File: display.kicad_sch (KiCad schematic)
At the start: 42 parts, among them J301 FPC24(0.5MM), J302 FPC10(0.5MM), Q301 2N7002, Q302 2N7002, Q303 AO3401A

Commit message: Pre routing: footprints&parts
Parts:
- D301, D302, D303, D304, D305, D306: JLCPCB (none) -> C965863
- D307, D308, D309: value MDD SS14 -> B5819W; footprint Diode_SMD:D_SMA -> Diode_SMD:D_SOD-123; JLCPCB C2480 -> C8598
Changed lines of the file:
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@@
       (effects (font (size 1.27 1.27)) hide)
     )
-    (property "JLCPCB" "" (id 4) (at 78.105 140.97 0)
+    (property "JLCPCB" "C965863" (id 4) (at 78.105 140.97 0)
       (effects (font (size 1.27 1.27)) hide)
     )
@@
       (effects (font (size 1.27 1.27)) hide)
     )
-    (property "JLCPCB" "" (id 4) (at 78.105 62.23 0)
+    (property "JLCPCB" "C965863" (id 4) (at 78.105 62.23 0)
       (effects (font (size 1.27 1.27)) hide)
     )
@@
     (in_bom yes) (on_board yes)
     (property "Reference" "D308" (id 0) (at 171.45 49.403 0))
-    (property "Value" "MDD SS14" (id 1) (at 174.244 44.958 0))
-    (property "Footprint" "Diode_SMD:D_SMA" (id 2) (at 171.45 46.99 0)
-      (effects (font (size 1.27 1.27)) hide)
-    )
-    (property "Datasheet" "https://datasheet.lcsc.com/lcsc/2204121115_MDD-Microdiode-Electronics--SS14_C2480.pdf" (id 3) (at 171.45 46.99 0)
-      (effects (font (size 1.27 1.27)) hide)
-    )
-    (property "JLCPCB" "C2480" (id 4) (at 171.45 46.99 0)
+    (property "Value" "B5819W" (id 1) (at 174.244 44.958 0))
+    (property "Footprint" "Diode_SMD:D_SOD-123" (id 2) (at 171.45 46.99 0)
+      (effects (font (size 1.27 1.27)) hide)
+    )
+    (property "Datasheet" "" (id 3) (at 171.45 46.99 0)
+      (effects (font (size 1.27 1.27)) hide)
+    )
+    (property "JLCPCB" "C8598 " (id 4) (at 171.45 46.99 0)
       (effects (font (size 1.27 1.27)) hide)
     )
@@
     (in_bom yes) (on_board yes)
     (property "Reference" "D307" (id 0) (at 162.56 74.93 90))
-    (property "Value" "MDD SS14" (id 1) (at 166.37 72.39 90))
-    (property "Footprint" "Diode_SMD:D_SMA" (id 2) (at 160.02 72.39 0)
-      (effects (font (size 1.27 1.27)) hide)
-    )
-    (property "Datasheet" "https://datasheet.lcsc.com/lcsc/2204121115_MDD-Microdiode-Electronics--SS14_C2480.pdf" (id 3) (at 160.02 72.39 0)
-      (effects (font (size 1.27 1.27)) hide)
-    )
-    (property "JLCPCB" "C2480" (id 4) (at 160.02 72.39 0)
+    (property "Value" "B5819W" (id 1) (at 166.37 72.39 90))
+    (property "Footprint" "Diode_SMD:D_SOD-123" (id 2) (at 160.02 72.39 0)
+      (effects (font (size 1.27 1.27)) hide)
+    )
+    (property "Datasheet" "" (id 3) (at 160.02 72.39 0)
+      (effects (font (size 1.27 1.27)) hide)
+    )
+    (property "JLCPCB" "C8598 " (id 4) (at 160.02 72.39 0)
       (effects (font (size 1.27 1.27)) hide)
     )
@@
       (effects (font (size 1.27 1.27)) hide)
     )
-    (property "JLCPCB" "" (id 4) (at 107.315 62.23 0)
+    (property "JLCPCB" "C965863" (id 4) (at 107.315 62.23 0)
       (effects (font (size 1.27 1.27)) hide)
     )
@@
       (effects (font (size 1.27 1.27)) hide)
     )
-    (property "JLCPCB" "" (id 4) (at 92.71 140.97 0)
+    (property "JLCPCB" "C965863" (id 4) (at 92.71 140.97 0)
       (effects (font (size 1.27 1.27)) hide)
     )
@@
       (effects (font (size 1.27 1.27)) hide)
     )
-    (property "JLCPCB" "" (id 4) (at 92.71 62.23 0)
+    (property "JLCPCB" "C965863" (id 4) (at 92.71 62.23 0)
       (effects (font (size 1.27 1.27)) hide)
     )
@@
     (in_bom yes) (on_board yes)
     (property "Reference" "D309" (id 0) (at 172.085 69.85 0))
-    (property "Value" "MDD SS14" (id 1) (at 174.371 65.151 0))
-    (property "Footprint" "Diode_SMD:D_SMA" (id 2) (at 171.45 67.31 0)
-      (effects (font (size 1.27 1.27)) hide)
-    )
-    (property "Datasheet" "https://datasheet.lcsc.com/lcsc/2204121115_MDD-Microdiode-Electronics--SS14_C2480.pdf" (id 3) (at 171.45 67.31 0)
-      (effects (font (size 1.27 1.27)) hide)
-    )
-    (property "JLCPCB" "C2480" (id 4) (at 171.45 67.31 0)
+    (property "Value" "B5819W" (id 1) (at 174.371 65.151 0))
+    (property "Footprint" "Diode_SMD:D_SOD-123" (id 2) (at 171.45 67.31 0)
+      (effects (font (size 1.27 1.27)) hide)
+    )
+    (property "Datasheet" "" (id 3) (at 171.45 67.31 0)
+      (effects (font (size 1.27 1.27)) hide)
+    )
+    (property "JLCPCB" "C8598 " (id 4) (at 171.45 67.31 0)
       (effects (font (size 1.27 1.27)) hide)
     )
@@
       (effects (font (size 1.27 1.27)) hide)
     )
-    (property "JLCPCB" "" (id 4) (at 107.315 140.97 0)
-      (effects (font (size 1.27 1.27)) hide)
-    )
+    (property "JLCPCB" "C965863" (id 4) (at 107.315 140.97 0)
+      (effects (font (size 1.27 1.27)) hide)
+    )

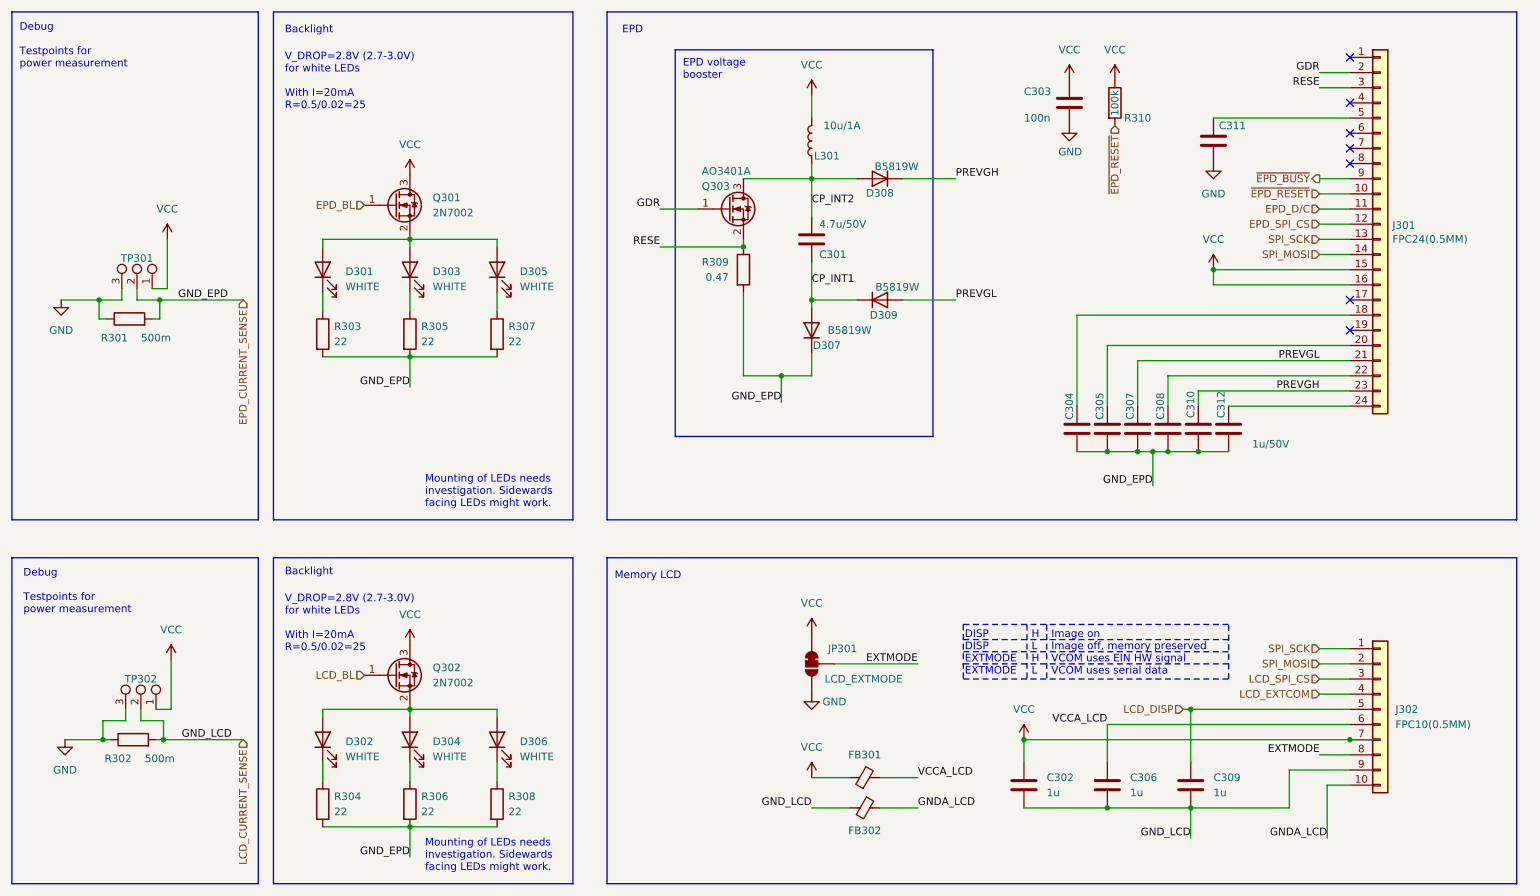
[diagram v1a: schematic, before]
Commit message: Schematics: Add mountingpins to connectors, remove ERC warnings for alternate parts
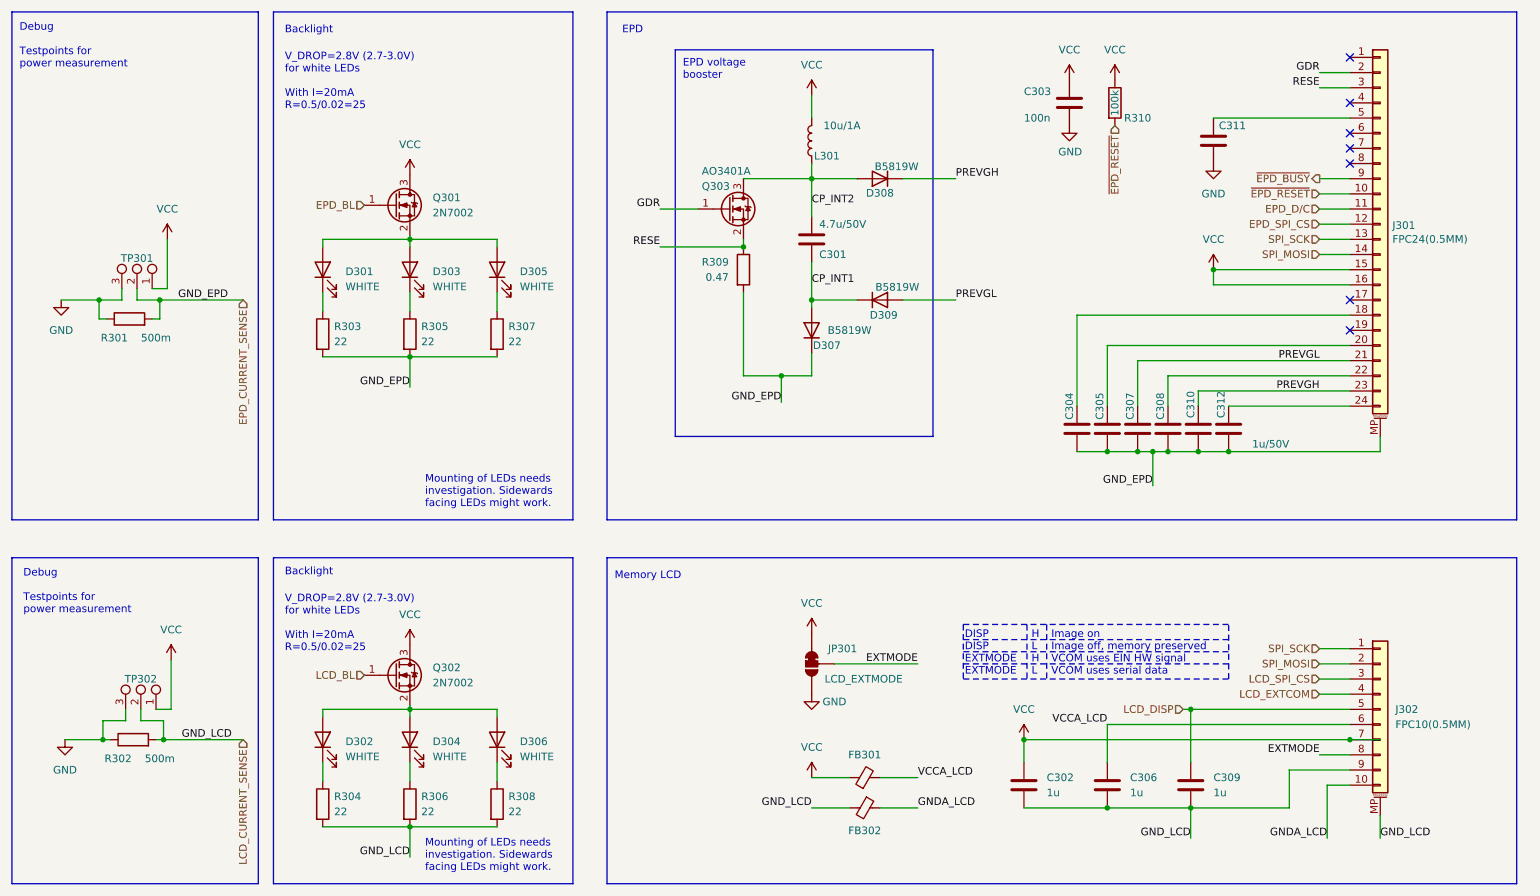
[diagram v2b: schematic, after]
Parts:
- D301, D302, D303, D304, D305, D306: footprint LED_SMD:LED_0805_2012Metric -> project-lib:LED_sidemount
- J301: symbol Connector_Generic:Conn_01x24 -> Connector_Generic_MountingPin:Conn_01x24_MountingPin
- J302: symbol Connector_Generic:Conn_01x10 -> Connector_Generic_MountingPin:Conn_01x10_MountingPin
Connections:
- net EPD_CURRENT_SENSE: now also J301.MP (MountPin); no longer R304.2, R306.2, R308.2
- net LCD_CURRENT_SENSE: now also J302.MP (MountPin), R304.2, R306.2, R308.2
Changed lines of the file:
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@@
   (junction (at 217.17 92.71) (diameter 0) (color 0 0 0 0)
+  )
+  (junction (at 229.87 92.71) (diameter 0) (color 0 0 0 0)
   )
   (junction (at 219.71 92.71) (diameter 0) (color 0 0 0 0)
@@
     (stroke (width 0) (type default) (color 0 0 0 0))
   )
+  (wire (pts (xy 255.27 90.17) (xy 255.27 92.71))
+    (stroke (width 0) (type default) (color 0 0 0 0))
+  )
   (polyline (pts (xy 125.73 19.05) (xy 125.73 104.14))
     (stroke (width 0) (type default) (color 0 0 0 0))
@@
     (stroke (width 0) (type default) (color 0 0 0 0))
   )
+  (wire (pts (xy 255.27 153.67) (xy 255.27 157.48))
+    (stroke (width 0) (type default) (color 0 0 0 0))
+  )
   (wire (pts (xy 92.71 58.42) (xy 92.71 57.15))
     (stroke (width 0) (type default) (color 0 0 0 0))
@@
     (stroke (width 0) (type default) (color 0 0 0 0))
   )
+  (wire (pts (xy 255.27 92.71) (xy 229.87 92.71))
+    (stroke (width 0) (type default) (color 0 0 0 0))
+  )
   (polyline (pts (xy 137.16 25.4) (xy 180.34 25.4))
     (stroke (width 0) (type default) (color 0 0 0 0))
@@
     (effects (font (size 1.27 1.27)) (justify right bottom))
   )
-  (label "GND_EPD" (at 92.71 160.655 180)
+  (label "GND_LCD" (at 92.71 160.655 180)
     (effects (font (size 1.27 1.27)) (justify right bottom))
   )
@@
   (label "EXTMODE" (at 245.11 143.51 180)
     (effects (font (size 1.27 1.27)) (justify right bottom))
+  )
+  (label "GND_LCD" (at 255.27 157.48 0)
+    (effects (font (size 1.27 1.27)) (justify left bottom))
   )
   (label "PREVGH" (at 245.11 82.55 180)
@@
       (effects (font (size 1.27 1.27)) (justify right))
     )
-    (property "Footprint" "LED_SMD:LED_0805_2012Metric" (id 2) (at 78.105 140.97 0)
+    (property "Footprint" "project-lib:LED_sidemount" (id 2) (at 78.105 140.97 0)
       (effects (font (size 1.27 1.27)) hide)
     )
@@
       (effects (font (size 1.27 1.27)) (justify right))
     )
-    (property "Footprint" "LED_SMD:LED_0805_2012Metric" (id 2) (at 78.105 62.23 0)
+    (property "Footprint" "project-lib:LED_sidemount" (id 2) (at 78.105 62.23 0)
       (effects (font (size 1.27 1.27)) hide)
     )
@@
     (pin "2")
   )
-  (symbol (lib_id "Connector_Generic:Conn_01x24") (at 255.27 54.61 0) (unit 1)
+  (symbol (lib_id "Connector_Generic_MountingPin:Conn_01x24_MountingPin") (at 255.27 54.61 0) (unit 1)
     (in_bom yes) (on_board yes)
     (property "Reference" "J301" (id 0) (at 257.302 54.8132 0)
@@
     (pin "8")
     (pin "9")
+    (pin "MP")
   )
   (symbol (lib_id "Transistor_FET:2N7002") (at 90.17 130.175 0) (unit 1)
@@
       (effects (font (size 1.27 1.27)) (justify right))
     )
-    (property "Footprint" "LED_SMD:LED_0805_2012Metric" (id 2) (at 107.315 62.23 0)
+    (property "Footprint" "project-lib:LED_sidemount" (id 2) (at 107.315 62.23 0)
       (effects (font (size 1.27 1.27)) hide)
     )
@@
       (effects (font (size 1.27 1.27)) (justify right))
     )
-    (property "Footprint" "LED_SMD:LED_0805_2012Metric" (id 2) (at 92.71 140.97 0)
+    (property "Footprint" "project-lib:LED_sidemount" (id 2) (at 92.71 140.97 0)
       (effects (font (size 1.27 1.27)) hide)
     )
@@
       (effects (font (size 1.27 1.27)) (justify right))
     )
-    (property "Footprint" "LED_SMD:LED_0805_2012Metric" (id 2) (at 92.71 62.23 0)
+    (property "Footprint" "project-lib:LED_sidemount" (id 2) (at 92.71 62.23 0)
       (effects (font (size 1.27 1.27)) hide)
     )
@@
     (pin "2")
   )
-  (symbol (lib_id "Connector_Generic:Conn_01x10") (at 255.27 135.89 0) (unit 1)
+  (symbol (lib_id "Connector_Generic_MountingPin:Conn_01x10_MountingPin") (at 255.27 135.89 0) (unit 1)
     (in_bom yes) (on_board yes) (fields_autoplaced)
     (property "Reference" "J302" (id 0) (at 257.81 135.8899 0)
@@
     (pin "8")
     (pin "9")
+    (pin "MP")
   )
   (symbol (lib_id "power:VCC") (at 52.07 57.15 0) (unit 1)
@@
       (effects (font (size 1.27 1.27)) (justify right))
     )
-    (property "Footprint" "LED_SMD:LED_0805_2012Metric" (id 2) (at 107.315 140.97 0)
-      (effects (font (size 1.27 1.27)) hide)
-    )
+    (property "Footprint" "project-lib:LED_sidemount" (id 2) (at 107.315 140.97 0)
+      (effects (font (size 1.27 1.27)) hide)
+    )

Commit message: schematic: replace LCD Light with connector for Azumo light panel
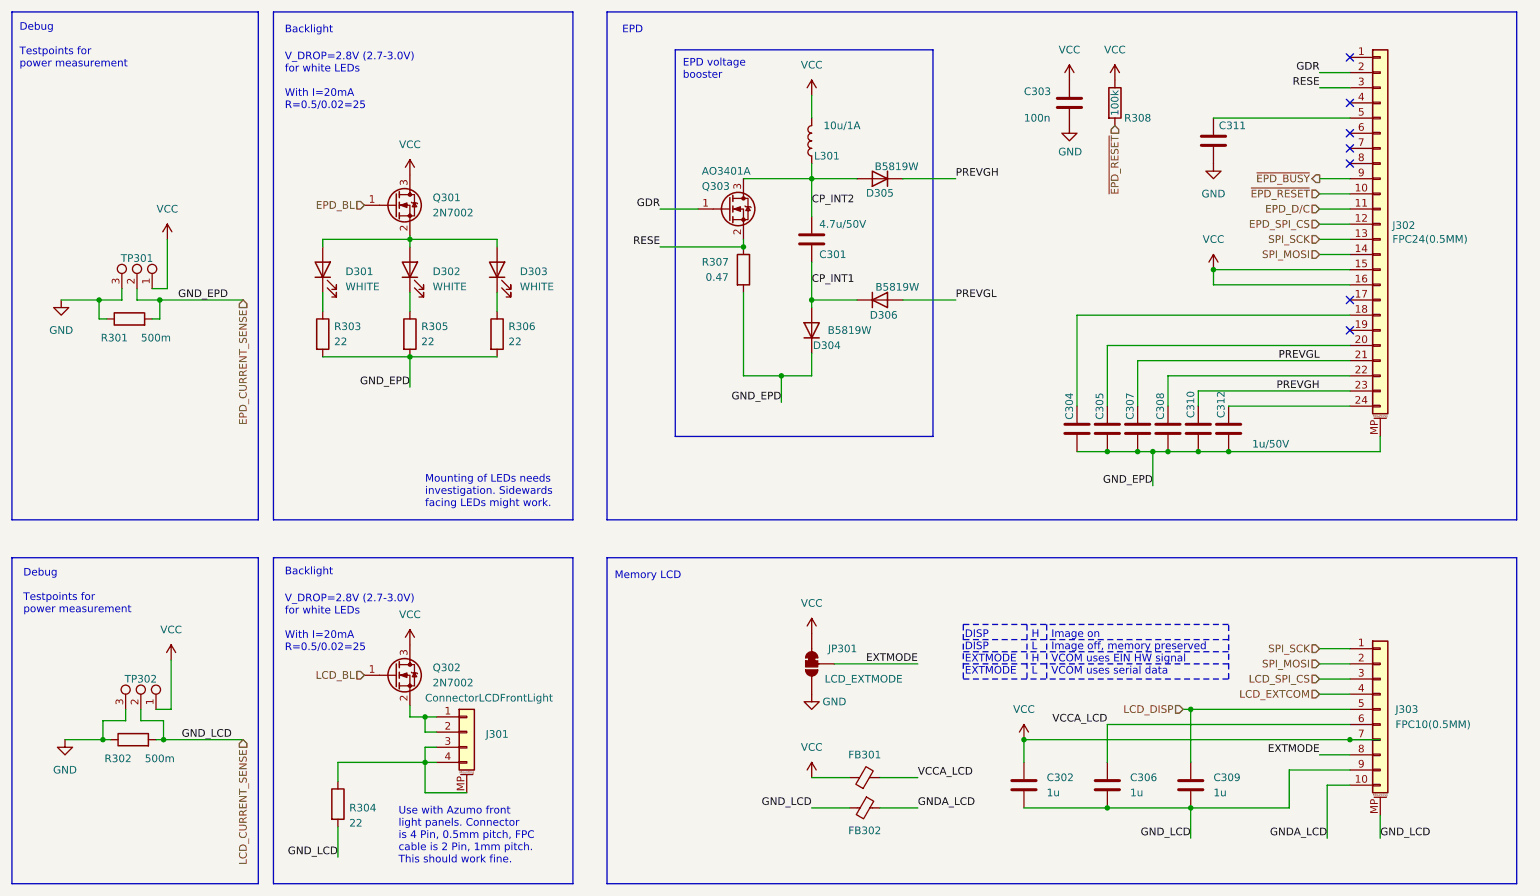
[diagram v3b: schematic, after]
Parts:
- removed D302, D304, D306: WHITE, project-lib:LED_sidemount, symbol Device:LED
- removed R304, R308: 22, Resistor_SMD:R_0603_1608Metric, symbol Device:R
- added J301: ConnectorLCDFrontLight, project-lib:jlcpcb-C11047_FFC_1x04-1MP_P0.50mm_Horizontal, symbol Connector_Generic_MountingPin:Conn_01x04_MountingPin
- renumbered D303 to D302, D305 to D303, D307 to D304, D308 to D305, D309 to D306, J301 to J302, J302 to J303, R306 to R304, R307 to R306, R309 to R307, R310 to R308
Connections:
- net at Q302.2 (S): now also J301.1 (Pin_1), J301.2 (Pin_2)
- net at R304.1: now also J301.3 (Pin_3), J301.4 (Pin_4), J301.MP (MountPin)
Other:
- note added: "Use with Azumo front light panels. Connector is 4 Pin, 0.5mm pitch, FPC cable is 2 Pin, 1mm pitch. This should work fine."
- moved on the sheet: R304
